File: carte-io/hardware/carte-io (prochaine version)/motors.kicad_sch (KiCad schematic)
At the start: 30 parts, among them J4 JST_PH_B4B, J5 JST_PH_B4B, J6 JST_PH_B4B, J7 JST_PH_B4B, J8 TSW-104-07-G-T, J9 TSW-104-07-G-T, U10 CM1293A-04SO, U11 74LVC125APW, U4 CM1293A-04SO, U5 TXU0104PWR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

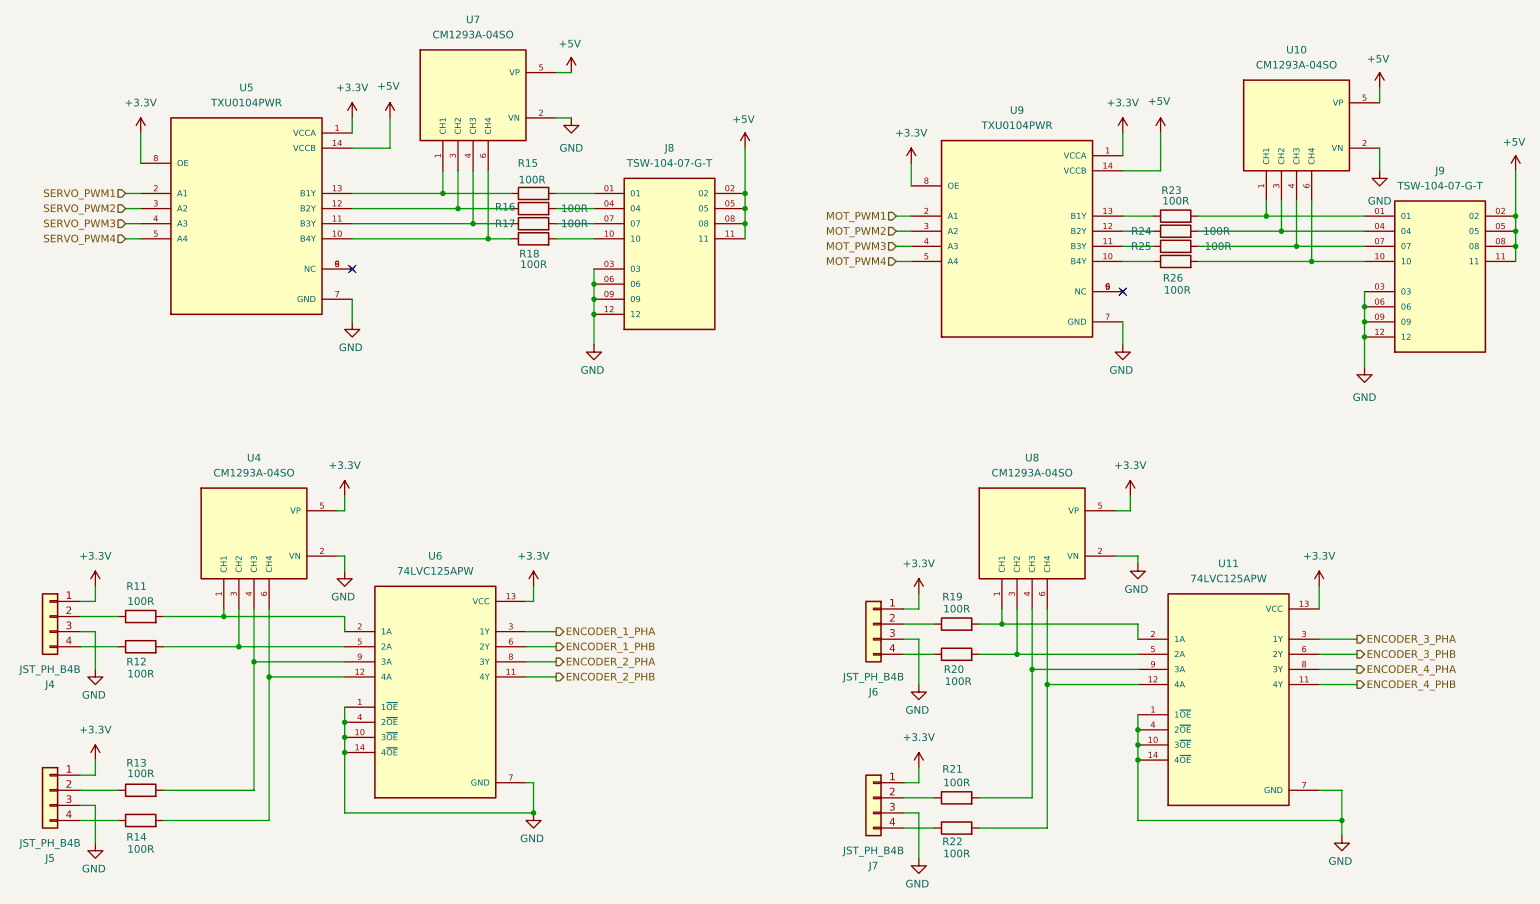
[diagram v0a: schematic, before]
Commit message: Commit de sauvegarde, gros changement sur la carte IO, les connecteurs sont compatibles SeeedStudio Grove. Il faut reprendre une grosse partie du routage et rajouter deux entrées analogiques
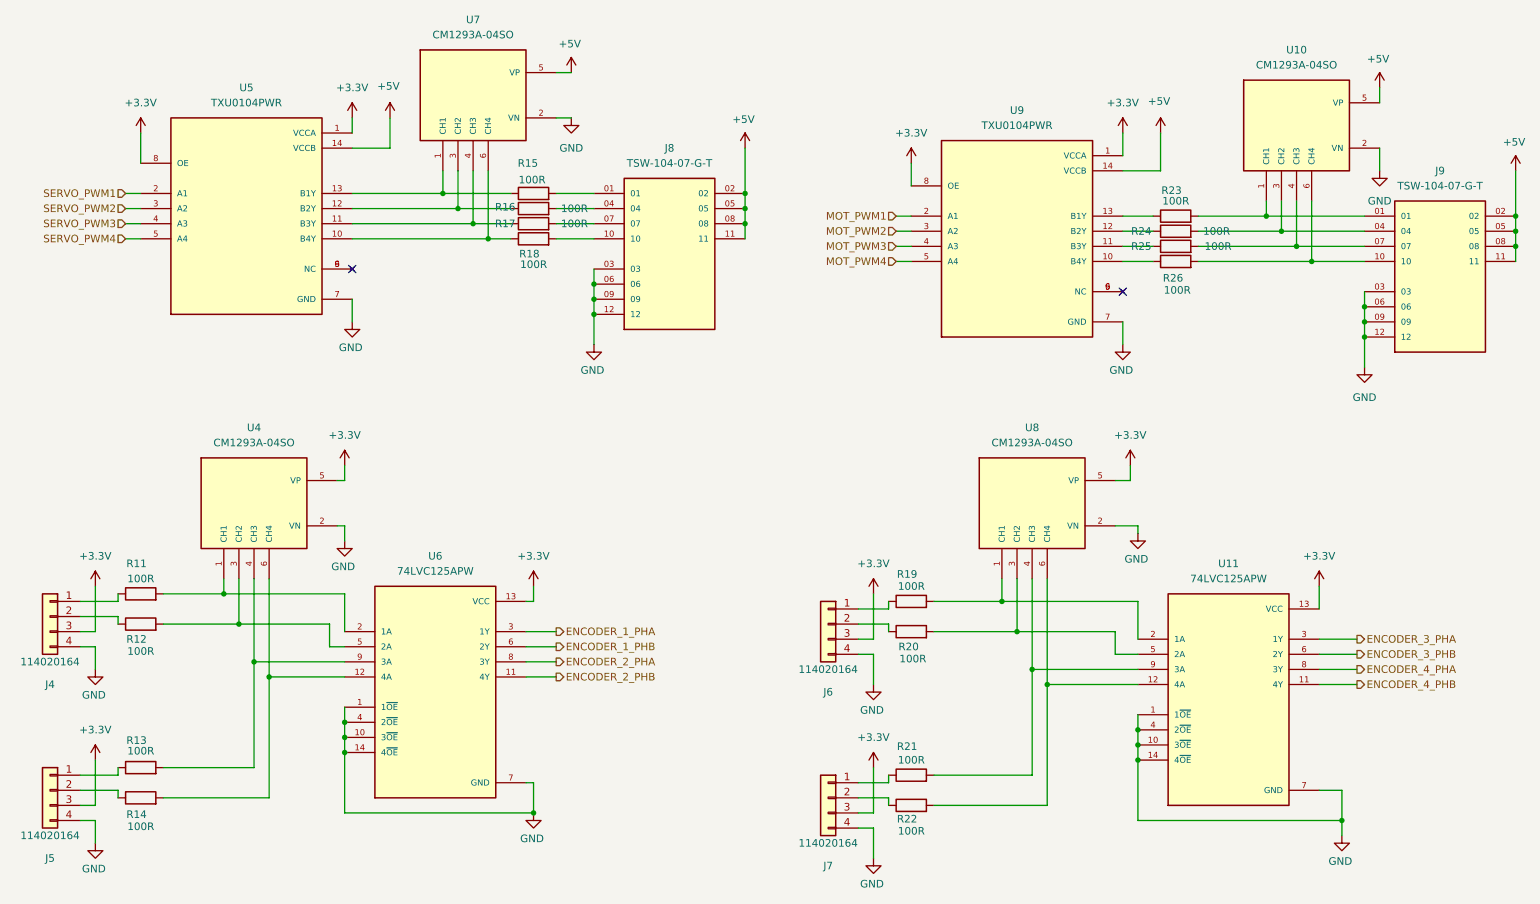
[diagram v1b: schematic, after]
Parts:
- J4, J5, J6, J7: value JST_PH_B4B -> 114020164; footprint Connector_JST:JST_PH_B4B-PH-K_1x04_P2.00mm_Vertical -> SeeedStudio - Horizontal Header -114020164:SEEEDSTUDIO_114020164; symbol Connector_Generic:Conn_01x04 -> SeeedStudio - Horizontal header:SeeedStudio - 114020164 - R/A
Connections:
- net +3.3V: now also J4.3 (Pin_3), J5.3 (Pin_3), J6.3 (Pin_3), J7.3 (Pin_3); no longer J4.1 (Pin_1), J5.1 (Pin_1), J6.1 (Pin_1), J7.1 (Pin_1)
- net GND: now also J4.4 (Pin_4), J5.4 (Pin_4), J6.4 (Pin_4), J7.4 (Pin_4); no longer J4.3 (Pin_3), J5.3 (Pin_3), J6.3 (Pin_3), J7.3 (Pin_3)
- net at R21.1: now also J7.1 (Pin_1); no longer J7.2 (Pin_2)
- net at R22.1: now also J7.2 (Pin_2); no longer J7.4 (Pin_4)
- net at R12.1: now also J4.2 (Pin_2); no longer J4.4 (Pin_4)
- net at R13.1: now also J5.1 (Pin_1); no longer J5.2 (Pin_2)
- net at R14.1: now also J5.2 (Pin_2); no longer J5.4 (Pin_4)
- net at R11.1: now also J4.1 (Pin_1); no longer J4.2 (Pin_2)
- net at R19.1: now also J6.1 (Pin_1); no longer J6.2 (Pin_2)
- net at R20.1: now also J6.2 (Pin_2); no longer J6.4 (Pin_4)
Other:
- moved on the sheet: J6, J7, R11, R12, R13, R14, R19, R20, R21, R22, U4, U8
